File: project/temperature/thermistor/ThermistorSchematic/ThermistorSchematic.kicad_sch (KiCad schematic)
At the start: 12 parts, among them U1 MCP601, U2 MCP601

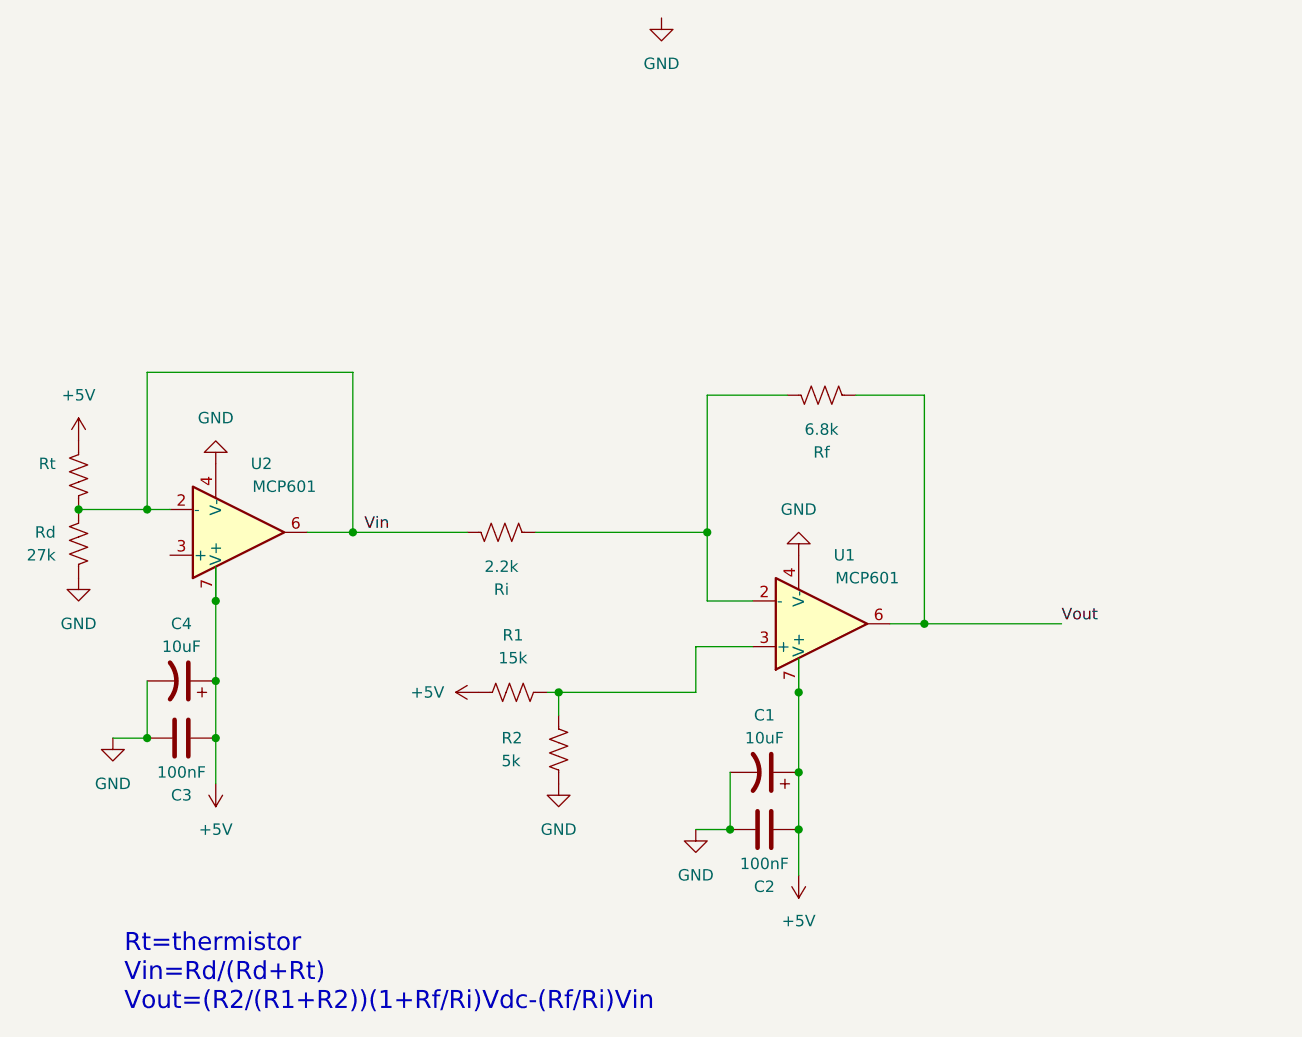
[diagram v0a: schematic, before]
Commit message: update to thermistor circuit
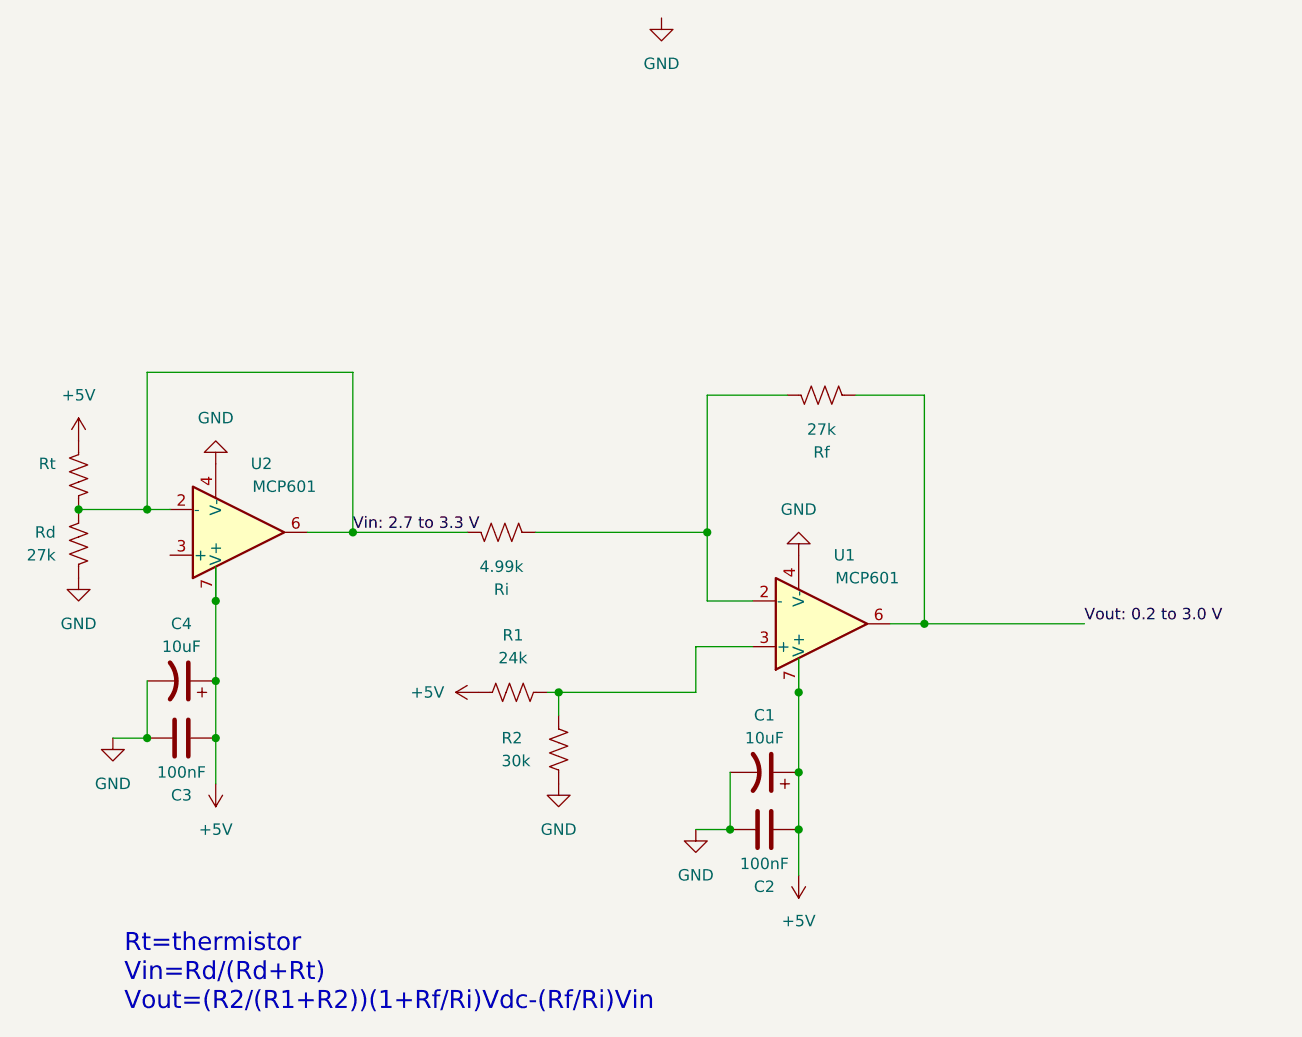
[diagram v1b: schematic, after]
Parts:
- R1: value 15k -> 24k
- R2: value 5k -> 30k
- Rf: value 6.8k -> 27k
- Ri: value 2.2k -> 4.99k
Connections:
- net Vin renamed Vin: 2.7  to 3.3 V
- net Vout renamed Vout: 0.2 to 3.0 V
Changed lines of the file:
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@@
     (stroke (width 0) (type default))
   )
-  (wire (pts (xy 180.34 104.14) (xy 195.58 104.14))
+  (wire (pts (xy 180.34 104.14) (xy 198.12 104.14))
     (stroke (width 0) (type default))
   )
@@
     (effects (font (size 2 2)) (justify left bottom))
   )
-  (label "Vin" (at 118.11 93.98 0) (fields_autoplaced)
+  (label "Vin: 2.7  to 3.3 V" (at 116.84 93.98 0) (fields_autoplaced)
     (effects (font (size 1.27 1.27)) (justify left bottom))
   )
-  (label "Vout" (at 195.58 104.14 0) (fields_autoplaced)
+  (label "Vout: 0.2 to 3.0 V" (at 198.12 104.14 0) (fields_autoplaced)
     (effects (font (size 1.27 1.27)) (justify left bottom))
   )
@@
       (effects (font (size 1.27 1.27)))
     )
-    (property "Value" "15k" (at 134.62 107.95 90)
+    (property "Value" "24k" (at 134.62 107.95 90)
       (effects (font (size 1.27 1.27)))
     )
@@
       (effects (font (size 1.27 1.27)) (justify left))
     )
-    (property "Value" "5k" (at 133.35 119.38 0)
+    (property "Value" "30k" (at 133.35 119.38 0)
       (effects (font (size 1.27 1.27)) (justify left))
     )
@@
       (effects (font (size 1.27 1.27)))
     )
-    (property "Value" "6.8k" (at 168.91 82.55 90)
+    (property "Value" "27k" (at 168.91 82.55 90)
       (effects (font (size 1.27 1.27)))
     )
@@
       (effects (font (size 1.27 1.27)))
     )
-    (property "Value" "2.2k" (at 133.35 97.79 90)
-      (effects (font (size 1.27 1.27)))
-    )
+    (property "Value" "4.99k" (at 133.35 97.79 90)
+      (effects (font (size 1.27 1.27)))
+    )
